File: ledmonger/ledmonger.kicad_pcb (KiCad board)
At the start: 4 copper layers, 20 x 40 mm, 24 parts, among them J1 Conn_01x07, J2 Conn_01x07, U1 TLC5955, U2 LMZ34202

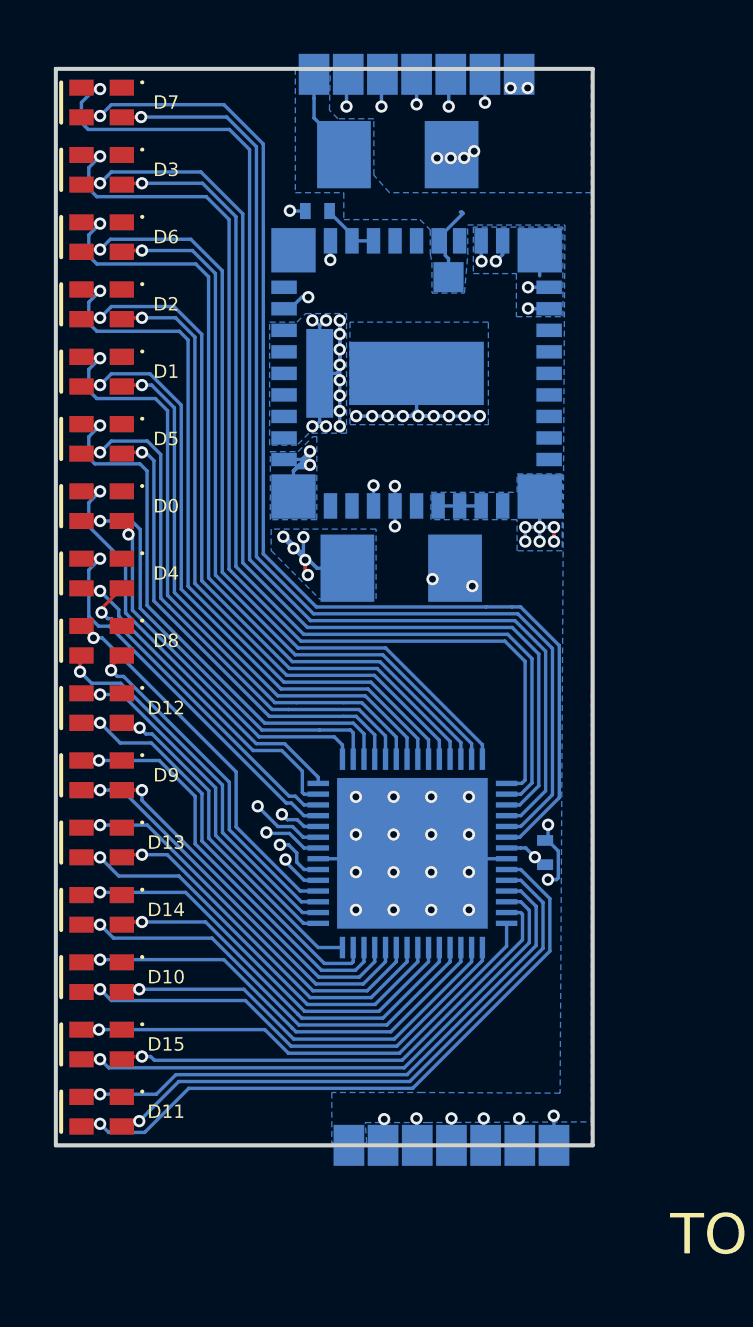
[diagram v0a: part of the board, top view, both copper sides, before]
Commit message: [ledmonger] Improved layout and added castellated connector.
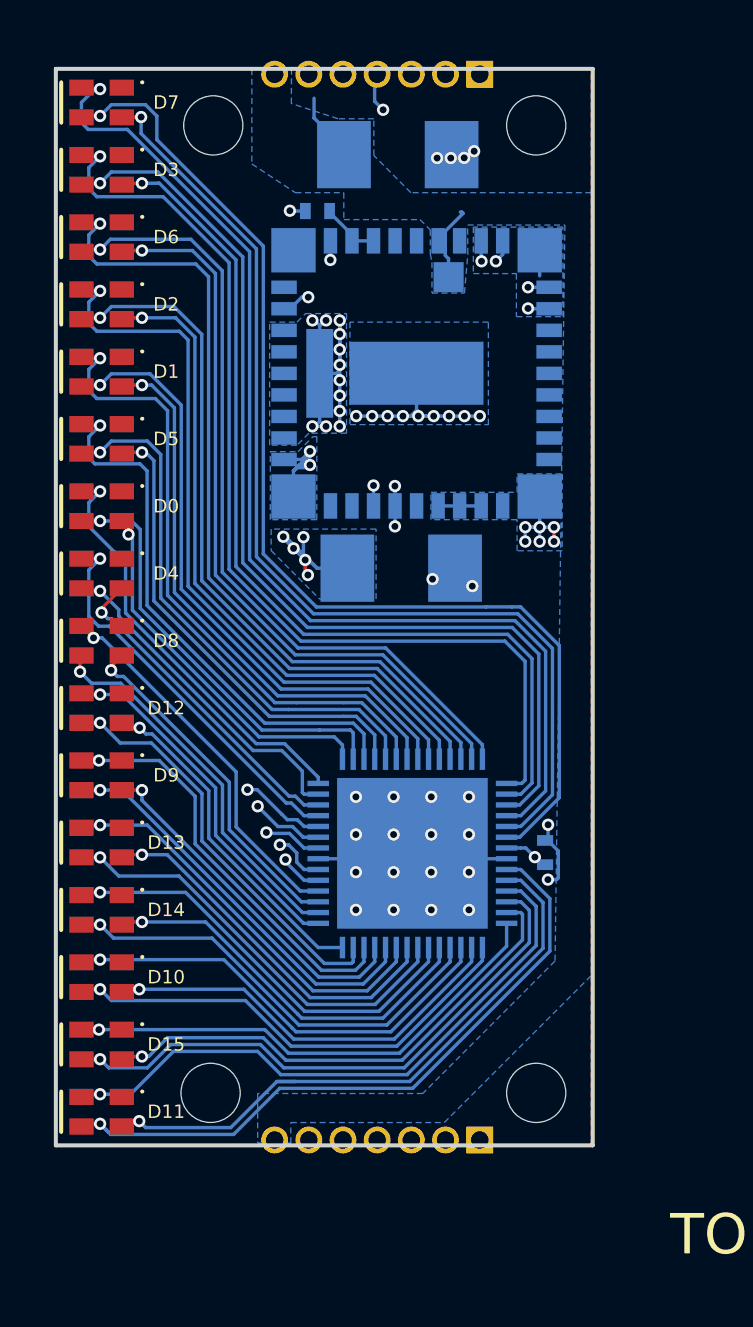
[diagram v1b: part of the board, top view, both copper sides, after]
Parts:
- added REF**: MountingHole_2.2mm_M2_ISO7380, Mounting_Holes:MountingHole_2.2mm_M2_ISO7380, F.Cu at (108.7, 34.6)
- added REF**: MountingHole_2.2mm_M2_ISO7380, Mounting_Holes:MountingHole_2.2mm_M2_ISO7380, F.Cu at (108.5, 70.5)
- added REF**: MountingHole_2.2mm_M2_ISO7380, Mounting_Holes:MountingHole_2.2mm_M2_ISO7380, F.Cu at (120.7, 70.5)
- added REF**: MountingHole_2.2mm_M2_ISO7380, Mounting_Holes:MountingHole_2.2mm_M2_ISO7380, F.Cu at (120.7, 34.6)
- J1: footprint NQBit:CONN_SMD_EDGE_x7_1.27mm_REV -> Pin_Headers:Pin_Header_Straight_1x07_Pitch1.27mm
- J2: footprint NQBit:CONN_SMD_EDGE_x7_1.27mm -> Pin_Headers:Pin_Header_Straight_1x07_Pitch1.27mm
- moved J2 2.35 mm to (118.5, 32.7), turned to 90 degrees
- moved J1 1.07 mm to (118.5, 72.3), turned to 90 degrees
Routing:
- net /SCLK: track 50.1 -> 45.5 mm, vias 3 -> 1
- net /GSCLK: track 52.4 -> 49.9 mm, vias 3 -> 1
- net /SOUT_LAST: track 41.9 -> 44.1 mm, vias 4 -> 2
- net /LEDB7: track 43.7 -> 41.5 mm
- net /LEDR7: track 40.8 -> 38.9 mm
- net /LEDG7: track 43.4 -> 41.7 mm
- net /SIN: track 16.6 -> 15.3 mm, vias 2 -> 1
- net GND: track 29.9 -> 28.8 mm, vias 49 -> 46
- net /LEDR3: track 35.9 -> 35.0 mm
- net /LEDB3: track 38.3 -> 37.4 mm
- net /LEDG3: track 38.6 -> 37.7 mm
- net /V36P0: track 6.26 -> 5.37 mm
- net /LEDR11: track 21.8 -> 22.6 mm
- net /LEDG15: track 20.9 -> 21.6 mm
- net /LEDB11: track 22.0 -> 22.7 mm
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
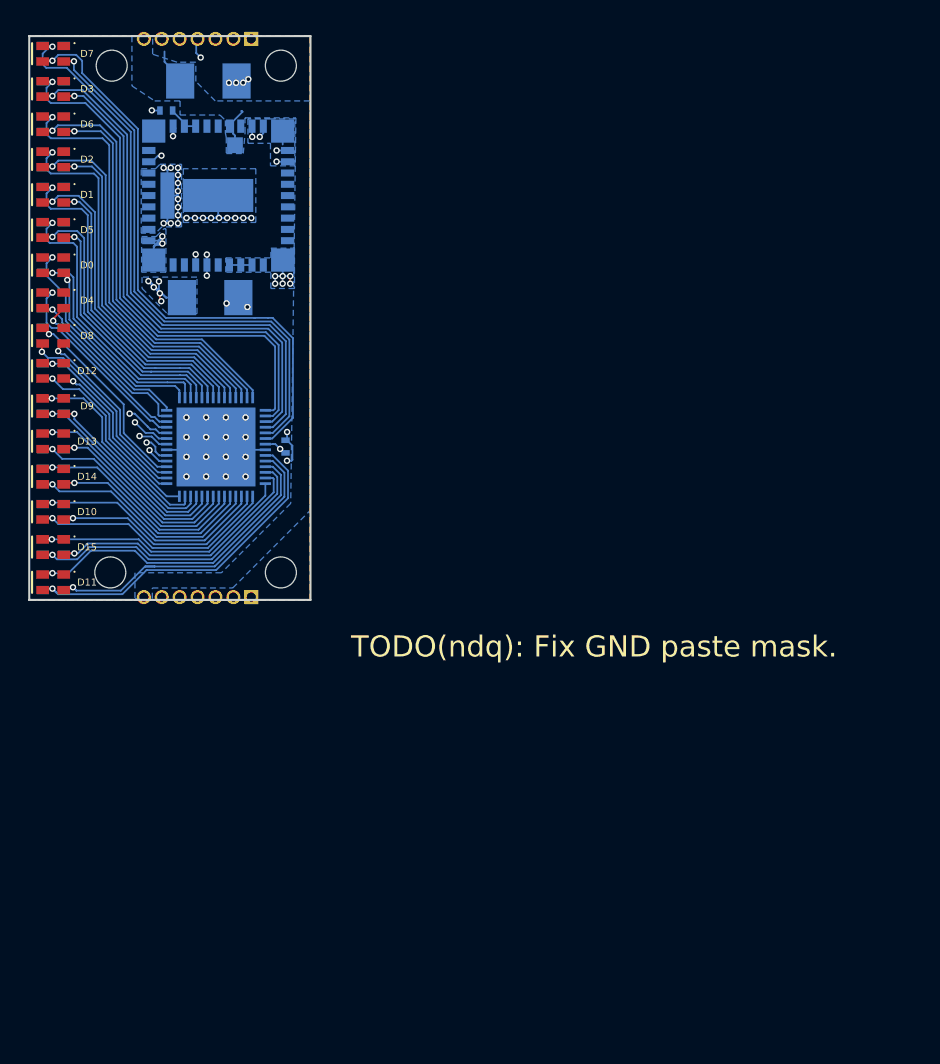
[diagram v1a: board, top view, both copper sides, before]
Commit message: [ledmonger] V1 ledmonger boards ordered.
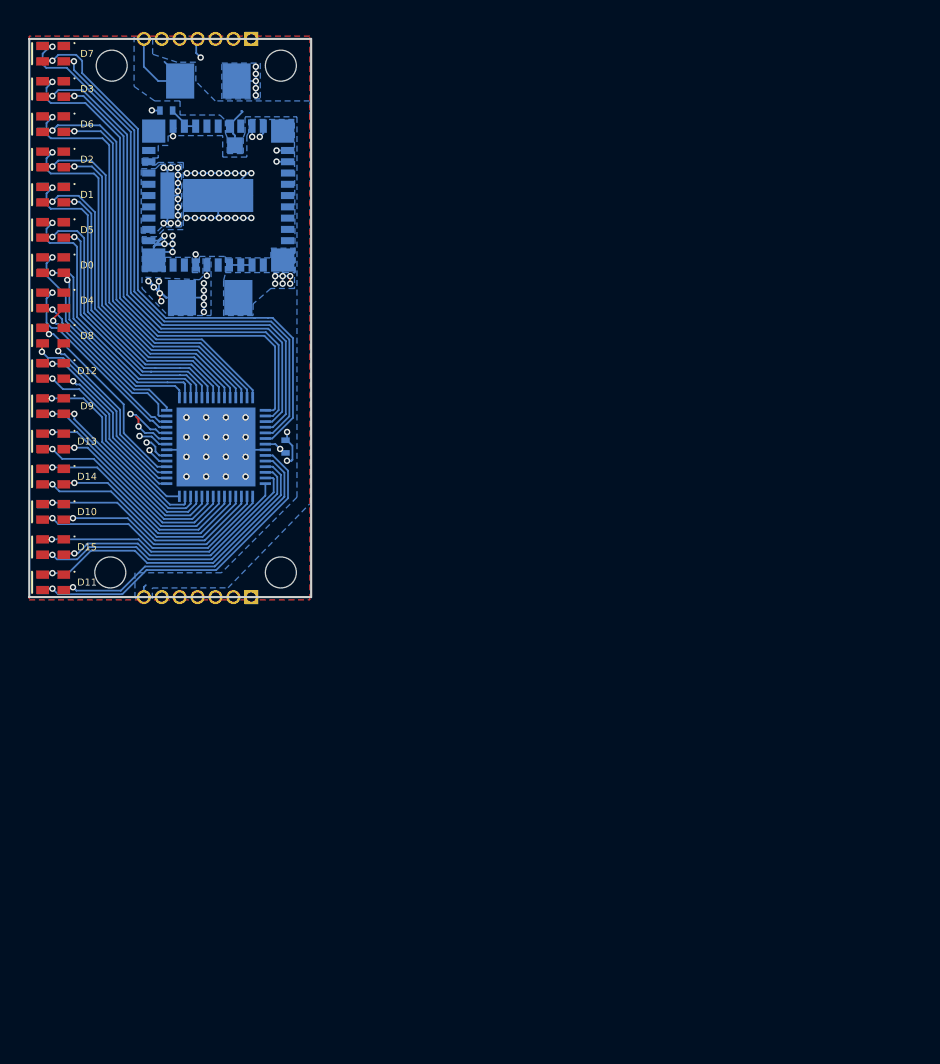
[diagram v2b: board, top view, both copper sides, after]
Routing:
- net GND: track 28.8 -> 55.0 mm, vias 46 -> 56
- net /V36P0: track 5.37 -> 10.5 mm
- net +3V3: track 21.9 -> 25.7 mm, vias 21 -> 25
- net /GSCLK: track 49.9 -> 46.5 mm
- net /LEDR11: track 22.6 -> 22.0 mm
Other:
- board size 20 x 40 mm -> 20 x 39.6 mm
- board text removed: "TODO(ndq): Fix GND paste mask."

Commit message: [ledmonger] Added silkscreen to connectors. [ledmonger] Added dimensions to fab drawing. [ledmonger] Fixed floating INH/UVLO, tied to PVIN. [ledmonger] Fixed default resistor value for VADJ to be 3.5V.
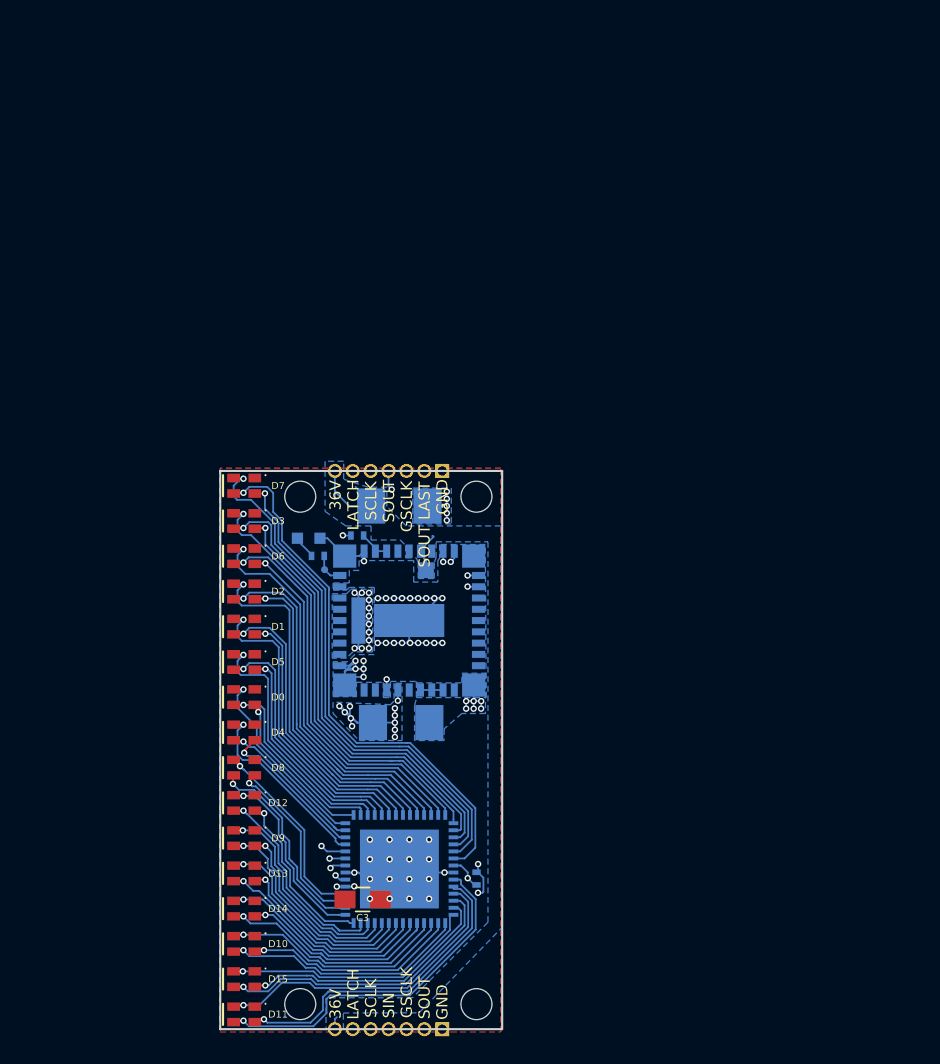
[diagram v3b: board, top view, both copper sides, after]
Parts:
- added C3: 100nF, Capacitors_SMD:C_0805_HandSoldering, F.Cu at (126.5, 93.8)
- added D16: LED_Small, LEDs:LED_0603, B.Cu at (122.6, 68.1)
- added R2: 8.06k, Resistors_SMD:R_0402_NoSilk, B.Cu at (123.3, 69.4)
- added TP0: PWRGD, NQBit:TEST_POINT_0.5mm, B.Cu at (123.8, 70.3)
- R1: value 8.87k -> 8.06k
- U1: footprint Housings_DFN_QFN:QFN-56-1EP_7x7mm_Pitch0.4mm -> NQBit:QFN-56-1EP_7x7mm_Pitch0.5mm
- moved REF** 33.6 mm to (134.5, 101.2)
- moved REF** 33.6 mm to (134.5, 65.2)
- moved D0 33.5 mm to (118.0, 79.4)
- moved D1 33.5 mm to (118.0, 74.4)
- moved D10 33.5 mm to (118.0, 96.9)
- moved D11 33.5 mm to (118.0, 101.9)
- moved D12 33.5 mm to (118.0, 86.9)
- moved D13 33.5 mm to (118.0, 91.9)
- moved D14 33.5 mm to (118.0, 94.4)
- moved D15 33.5 mm to (118.0, 99.4)
- moved D2 33.5 mm to (118.0, 71.9)
- moved D3 33.5 mm to (118.0, 66.9)
- moved D4 33.5 mm to (118.0, 81.9)
- moved D5 33.5 mm to (118.0, 76.9)
- moved D6 33.5 mm to (118.0, 69.4)
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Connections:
- net Net-(R1-Pad2) renamed /VADJ
- U2 pad 20: (no net) -> /PWRGD
- U2 pad 21: (no net) -> +3V3
- U2 pad 26: (no net) -> /V36P0
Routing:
- net /LEDB3: track 37.4 -> 31.9 mm
- net /LEDR3: track 35.0 -> 30.7 mm
- net /LEDG3: track 37.7 -> 33.6 mm
- net /LEDB7: track 41.5 -> 37.5 mm
- net /LEDR7: track 38.9 -> 35.3 mm
- net +3V3: track 25.7 -> 29.3 mm, vias 25 -> 26
- net /LEDG7: track 41.7 -> 38.4 mm
- net /LEDR0: track 13.9 -> 11.6 mm
- net /PWRGD: track 0.00 -> 2.24 mm
- net /LEDG0: track 16.1 -> 13.9 mm
- net /LEDB6: track 30.6 -> 28.5 mm
- net /LEDB5: track 20.4 -> 18.4 mm
- net /SCLK: track 45.7 -> 43.7 mm
- net /LEDB0: track 15.9 -> 13.9 mm
- net /LEDR6: track 27.7 -> 25.8 mm
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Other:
- board text added: "36V"
- board text added: "GND"
- board text added: "GSCLK"
- board text added: "LATCH"
- board text added: "SCLK"
- board text added: "SIN"
- board text added: "SOUT"
- board text added: "SOUT <-> SOUT_LAST"
- board text added: "SOUT LAST"
